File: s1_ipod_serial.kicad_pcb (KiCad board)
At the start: 2 copper layers, 21.6 x 49.5 mm, 32 parts, among them IC1 GL850G, J1 USB-MINIB-5PIN, P1 IPOD_CONNECTOR_MALE, U1 LM3526M-H, U2 FT232RL, X1 12 Mhz

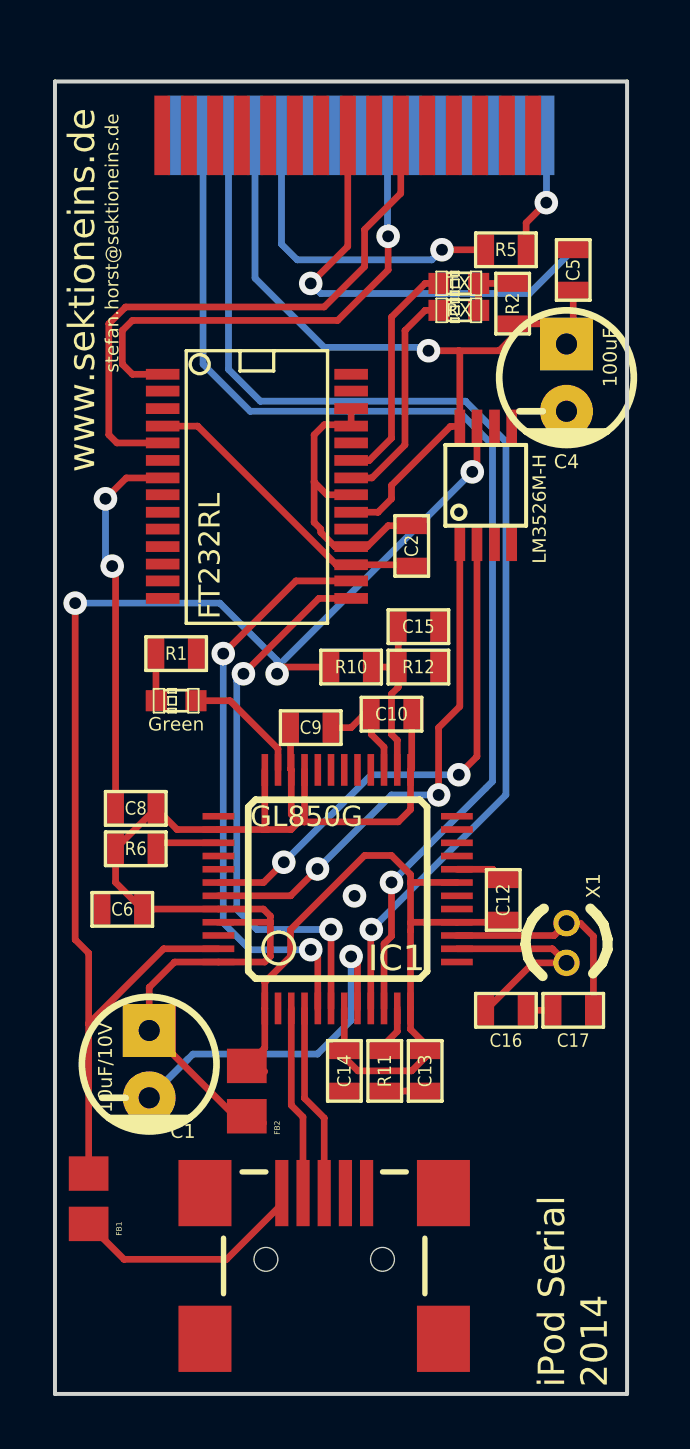
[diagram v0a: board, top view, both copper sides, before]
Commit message: new routing for usb, teileliste added, fix for selfpowered
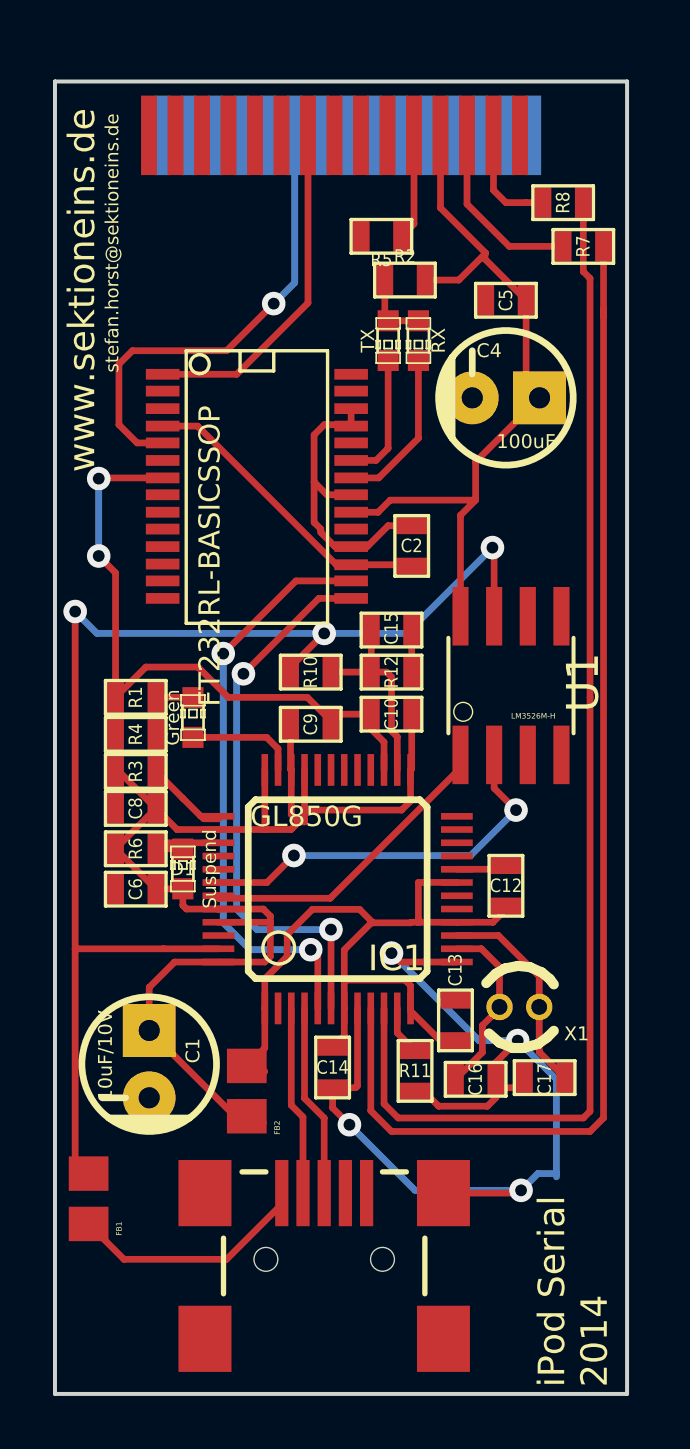
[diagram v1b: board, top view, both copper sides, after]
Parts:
- added D1: Suspend, LEDs.pretty:LED-0603, F.Cu at (139.4, 85.6)
- added R3: 0R, SMD_Packages.pretty:SM0603, F.Cu at (137.7, 81.9)
- added R4: 0R, SMD_Packages.pretty:SM0603, F.Cu at (137.7, 80.5)
- added R7: 0R, SMD_Packages.pretty:SM0603, F.Cu at (154.6, 62.1)
- added R8: 0R, SMD_Packages.pretty:SM0603, F.Cu at (153.8, 60.5)
- added SektionEinsLogo: VAL**, S1:SektionEinsLogo, B.Cu at (136.1, 54.4)
- P1: moved to B.Cu
- U1: footprint SSOP_Packages.pretty:SSOP-8 -> AWJLEagleLib:SO08
- U2: value FT232RL -> FT232RL-BASICSSOP
- moved U1 7.62 mm to (151.8, 78.7)
- moved R5 4.73 mm to (146.9, 61.7), turned to 0 degrees
- moved R2 4.16 mm to (147.8, 63.4), turned to 180 degrees
- moved D4 3.43 mm to (147.2, 65.7), turned to 270 degrees
- moved X1 3.00 mm to (152.1, 90.8), turned to 0 degrees
- moved C16 2.84 mm to (150.5, 93.5)
- moved C5 2.79 mm to (151.6, 64.1), turned to 0 degrees
- moved C17 2.76 mm to (153.1, 93.5)
- moved C4 2.41 mm to (151.6, 67.8), turned to 90 degrees
- moved R1 2.25 mm to (137.7, 79.1), turned to 180 degrees
- moved C13 2.22 mm to (149.7, 91.3), turned to 90 degrees
- moved D3 1.91 mm to (148.3, 65.7), turned to 270 degrees
- moved R10 1.54 mm to (144.3, 78.2)
- moved R11 1.14 mm to (148.2, 93.2)
- moved R12 1.03 mm to (147.3, 78.2)
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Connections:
- IC1 pad 37: GND -> Net-(IC1-Pad37)
- P1 pad 1: Net-(P1-Pad1) -> GND
- P1 pad 25: /IPOD_USB_D- -> Net-(P1-Pad25)
- P1 pad 27: /IPOD_USB_D+ -> Net-(P1-Pad27)
- R5 pad 1: Net-(P1-Pad1) -> GND
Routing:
- net GND: track 66.7 -> 79.1 mm, vias 4 -> 6
- net Net-(P1-Pad25): track 0.00 -> 8.34 mm
- net Net-(P1-Pad21): track 12.2 -> 4.00 mm, vias 1 -> 0
- net /PWREN1: track 19.7 -> 11.9 mm, vias 2 -> 0
- net /SERIAL_TX: track 19.0 -> 12.9 mm, vias 1 -> 0
- net Net-(IC1-Pad37): track 0.00 -> 5.12 mm
- net /OVCUR1: track 19.7 -> 14.8 mm
- net /SERIAL_RX: track 22.4 -> 17.7 mm, vias 0 -> 1
- net Net-(P1-Pad1): track 4.64 -> 0.00 mm, vias 1 -> 0
- net Net-(P1-Pad27): track 0.00 -> 4.13 mm
- net /SERIAL_TX_LED: track 8.76 -> 4.90 mm
- net VBUS: track 51.4 -> 48.9 mm
- net /IPOD_USB_D-: track 43.9 -> 46.3 mm, vias 1 -> 0
- net /SERIAL_RX_LED: track 8.46 -> 6.09 mm
- net /IPOD_USB_D+: track 43.8 -> 46.1 mm, vias 1 -> 0
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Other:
- net class Default: clearance 0.1 -> 0.153
- rule trace_clearance: 0.1 -> 0.153
- rule trace_min: 0.154 -> 0.254

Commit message: removed the 0R for self powered indicator, made fb 0608, rev. text added to board and sheet, routing optimized
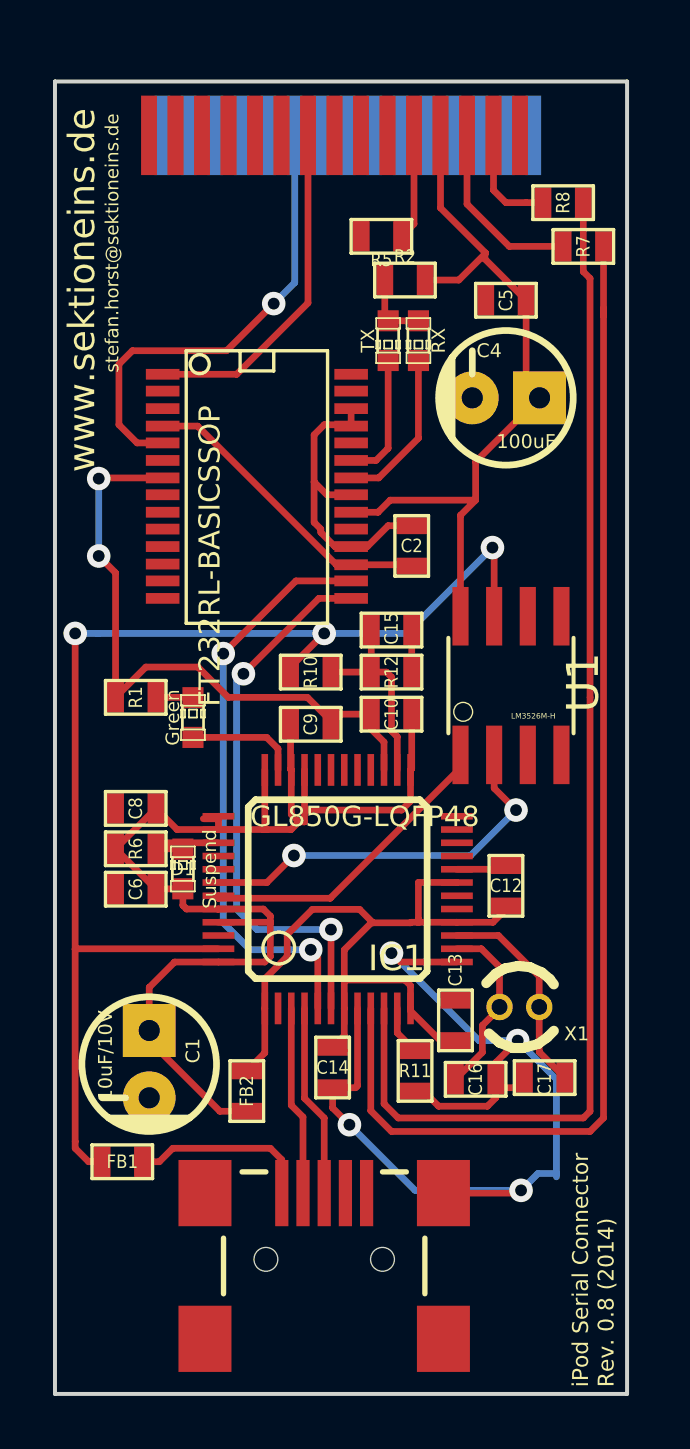
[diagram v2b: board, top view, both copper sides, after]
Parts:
- removed R3, R4: 0R, SMD_Packages.pretty:SM0603
- removed SektionEinsLogo: VAL**, S1:SektionEinsLogo
- FB1, FB2: footprint AWJLEagleLib:0805 -> SMD_Packages.pretty:SM0603
- IC1: value GL850G -> GL850G-LQFP48
- R1: value 480R -> 470R
- moved FB1 1.89 mm to (137.2, 96.6), turned to 180 degrees
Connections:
- IC1 pad 37: Net-(IC1-Pad37) -> DVDD
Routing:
- net Net-(IC1-Pad37): track 5.12 -> 0.00 mm
- net Net-(FB1-Pad1): track 9.29 -> 7.49 mm
- net VBUS: track 48.9 -> 48.1 mm
- net DVDD: track 49.5 -> 49.0 mm
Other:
- board text added: "iPod Serial Connector Rev. 0.8 (2014)"
- board text removed: "iPod Serial 2014"

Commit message: added current version
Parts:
- added SektionEinsLogo: VAL**, S1:SektionEinsLogo, B.Cu at (136.1, 54.4)
- C1: footprint Capacitors.pretty:CP_5x11mm -> SMD_Packages.pretty:SM0603
- C4: footprint Capacitors.pretty:CP_5x11mm -> SMD_Packages.pretty:SM1206
- C5: value 0,1uF -> 100nF
- U1: value LM3526M-H -> LM3526M-L
- moved C1 2.88 mm to (140.1, 90.8)
- moved FB2 1.33 mm to (141.5, 92.7), turned to 0 degrees
- moved C4 1.30 mm to (151.9, 66.5), turned to 180 degrees
- moved FB1 0.52 mm to (137.3, 96.1)
- moved X1 0.38 mm to (152.1, 90.4)
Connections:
- IC1 pad 24: GND -> (no net)
- IC1 pad 33: DVDD -> (no net)
- IC1 pad 36: DVDD -> (no net)
- IC1 pad 45: DVDD -> (no net)
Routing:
- net GND: track 79.1 -> 111.1 mm, vias 6 -> 9
- net DVDD: track 49.0 -> 35.4 mm
- net +5V: track 28.5 -> 30.9 mm
- net AVDD: track 29.2 -> 28.3 mm
- net VBUS: track 48.1 -> 47.4 mm
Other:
- board text added: "iPod Serial Connector Rev. 0.5 (2014)"
- board text removed: "iPod Serial Connector Rev. 0.8 (2014)"
